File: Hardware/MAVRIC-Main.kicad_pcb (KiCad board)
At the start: 2 copper layers, 0 parts

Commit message: Add basic connector and ChipKit headers
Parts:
- added J1: MTR1, CONN-WM6469CT, F.Cu at (72.4, 109.2)
- added J10: CAM, CONN-WM6469CT, F.Cu at (30.5, 66.0)
- added J11: CK-PWR, HDRV8W38P254_6X1-SMT, B.Cu at (90.2, 101.6)
- added J12: CK-A0, HDRV8W38P254_8X1-SMT, B.Cu at (110.5, 101.6)
- added J13: CK-A1, HDRV8W38P254_8X1-SMT, B.Cu at (133.3, 101.6)
- added J14: CK-COM, HDRV8W38P254_8X1-SMT, B.Cu at (128.3, 53.3)
- added J15: CK-D0, HDRV16W64P254_8X2-SMT, B.Cu at (105.4, 54.6)
- added J16: CK-X0, HDRV16W64P254_8X2-SMT, B.Cu at (146.1, 64.8)
- added J17: CK-D1, HDRV16W64P254_8X2-SMT, B.Cu at (83.6, 54.6)
- added J18: CK-X1, HDRV16W64P254_8X2-SMT, B.Cu at (146.1, 85.1)
- added J2: MTR4, CONN-WM6469CT, F.Cu at (95.2, 109.2)
- added J3: MTR2, CONN-WM6469CT, F.Cu at (118.1, 109.2)
- added J4: MTR5, CONN-WM6469CT, F.Cu at (72.4, 45.7)
- added J5: MTR3, CONN-WM6469CT, F.Cu at (95.2, 45.7)
- added J6: MTR6, CONN-WM6469CT, F.Cu at (118.1, 45.7)
- added J7: VID, CONN-WM6469CT, F.Cu at (141.0, 109.2)
- added J8: DAT, CONN-WM6469CT, F.Cu at (141.0, 45.7)
- added J9: ARM, CONN-WM6469CT, F.Cu at (30.5, 88.9)
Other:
- board outline added: 101.6 x 58.4 mm

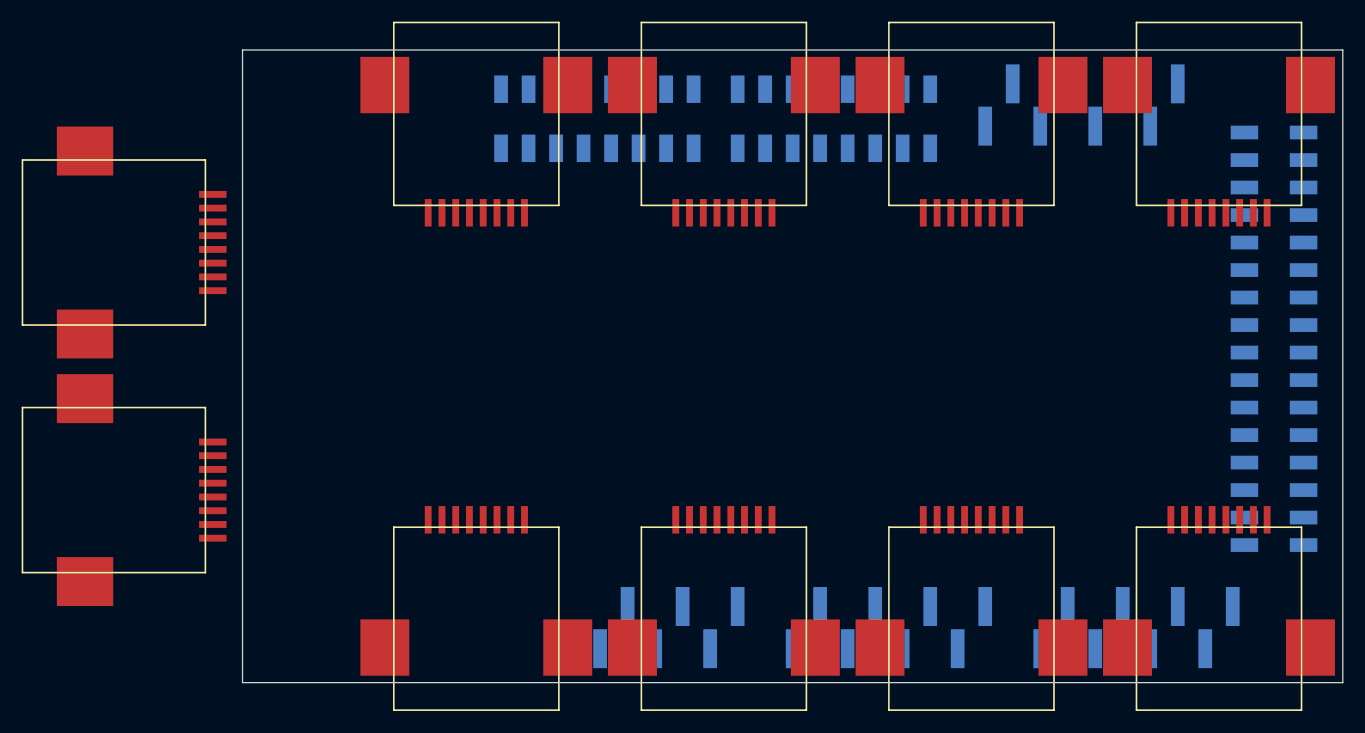
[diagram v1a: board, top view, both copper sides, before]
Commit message: Replace arm and camera connectors with vertical style
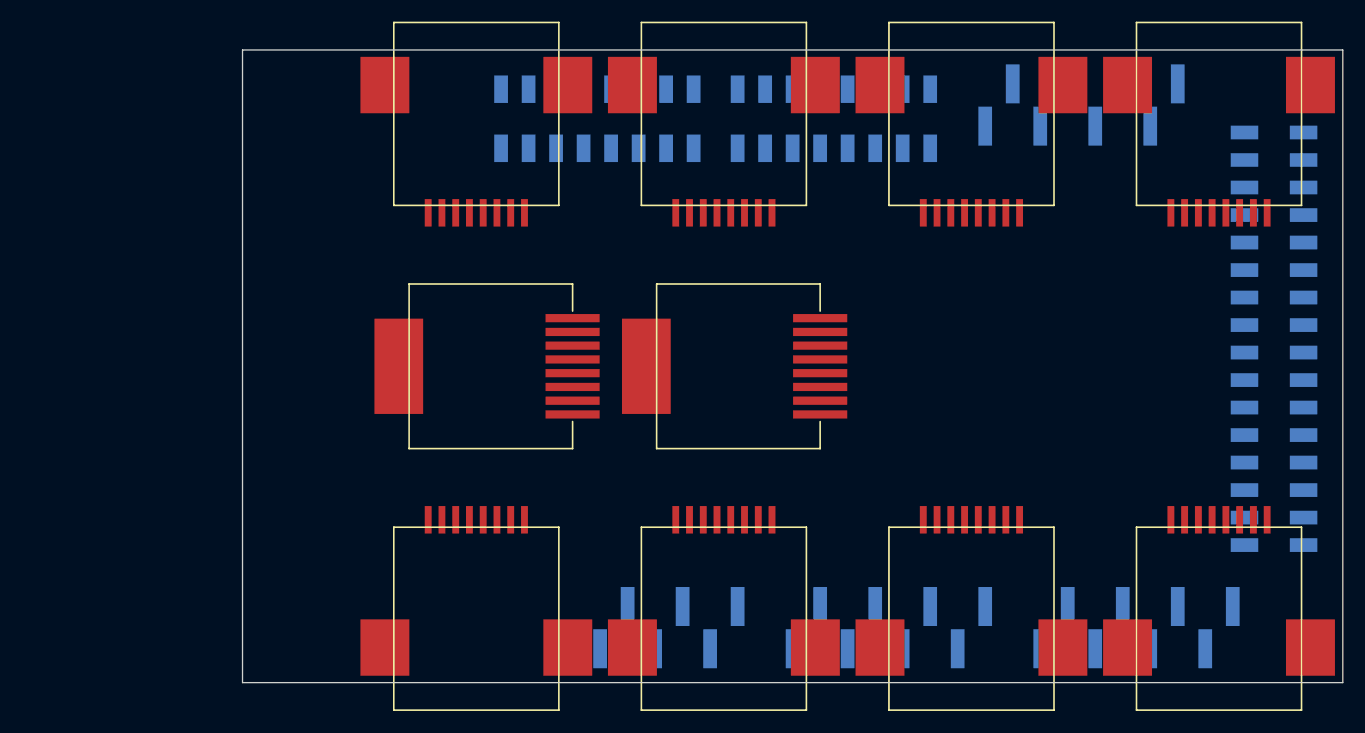
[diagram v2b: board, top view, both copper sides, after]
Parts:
- J10, J9: footprint CONN-WM6469CT -> CONN-WM3553CT
- moved J10 74.5 mm to (104.1, 77.5), turned to 90 degrees
- moved J9 52.1 mm to (81.3, 77.5), turned to 90 degrees
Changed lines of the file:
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@@
     (links 2)
     (no_connects 2)
-    (area 29.976 45.216 153.117474 109.724)
+    (area 50.749999 45.216 153.117474 109.724)
     (thickness 1.6)
     (drawings 4)
@@
     (mod_text_size 1 1)
     (mod_text_width 0.15)
-    (pad_size 1.27 3.6)
+    (pad_size 8.8 4.5)
     (pad_drill 0)
     (pad_to_mask_clearance 0)
@@
     )
   )
-  (module CONN-WM6469CT (layer F.Cu)
-    (at 30.48 88.9 270)
-    (descr "Conn, RJ45")
-    (tags Conn)
-    (fp_text reference J9 (at 0 -11.43 270) (layer F.SilkS) hide
-      (effects (font (size 1 1) (thickness 0.15)))
-    )
-    (fp_text value ARM (at 0 -12.7 270) (layer F.SilkS) hide
-      (effects (font (size 1 1) (thickness 0.15)))
-    )
-    (fp_line (start -7.62 0) (end -7.62 -16.891) (layer F.SilkS) (width 0.15))
-    (fp_line (start -7.62 -16.891) (end 7.62 -16.891) (layer F.SilkS) (width 0.15))
-    (fp_line (start 7.62 -16.891) (end 7.62 0) (layer F.SilkS) (width 0.15))
-    (fp_line (start 7.62 0) (end -7.62 0) (layer F.SilkS) (width 0.15))
-    (pad 1 smd rect (at -4.445 -17.5768 270) (size 0.635 2.54)
-      (layers F.Cu F.Paste F.Mask)
-    )
-    (pad 2 smd rect (at -3.175 -17.5768 270) (size 0.635 2.54)
-      (layers F.Cu F.Paste F.Mask)
-    )
-    (pad 3 smd rect (at -1.905 -17.5768 270) (size 0.635 2.54)
-      (layers F.Cu F.Paste F.Mask)
-    )
-    (pad 4 smd rect (at -0.635 -17.5768 270) (size 0.635 2.54)
-      (layers F.Cu F.Paste F.Mask)
-    )
-    (pad 5 smd rect (at 0.635 -17.5768 270) (size 0.635 2.54)
-      (layers F.Cu F.Paste F.Mask)
-    )
-    (pad 6 smd rect (at 1.905 -17.5768 270) (size 0.635 2.54)
-      (layers F.Cu F.Paste F.Mask)
-    )
-    (pad 7 smd rect (at 3.175 -17.5768 270) (size 0.635 2.54)
-      (layers F.Cu F.Paste F.Mask)
-    )
-    (pad 8 smd rect (at 4.445 -17.5768 270) (size 0.635 2.54)
-      (layers F.Cu F.Paste F.Mask)
-    )
-    (pad "" smd rect (at 8.4455 -5.7785 270) (size 4.5212 5.207)
-      (layers F.Cu F.Paste F.Mask)
-    )
-    (pad "" smd rect (at -8.4455 -5.7785 270) (size 4.5212 5.207)
-      (layers F.Cu F.Paste F.Mask)
-    )
-  )
-  (module CONN-WM6469CT (layer F.Cu)
-    (at 30.48 66.04 270)
-    (descr "Conn, RJ45")
-    (tags Conn)
-    (fp_text reference J10 (at 0 -11.43 270) (layer F.SilkS) hide
-      (effects (font (size 1 1) (thickness 0.15)))
-    )
-    (fp_text value CAM (at 0 -12.7 270) (layer F.SilkS) hide
-      (effects (font (size 1 1) (thickness 0.15)))
-    )
-    (fp_line (start -7.62 0) (end -7.62 -16.891) (layer F.SilkS) (width 0.15))
-    (fp_line (start -7.62 -16.891) (end 7.62 -16.891) (layer F.SilkS) (width 0.15))
-    (fp_line (start 7.62 -16.891) (end 7.62 0) (layer F.SilkS) (width 0.15))
-    (fp_line (start 7.62 0) (end -7.62 0) (layer F.SilkS) (width 0.15))
-    (pad 1 smd rect (at -4.445 -17.5768 270) (size 0.635 2.54)
-      (layers F.Cu F.Paste F.Mask)
-    )
-    (pad 2 smd rect (at -3.175 -17.5768 270) (size 0.635 2.54)
-      (layers F.Cu F.Paste F.Mask)
-    )
-    (pad 3 smd rect (at -1.905 -17.5768 270) (size 0.635 2.54)
-      (layers F.Cu F.Paste F.Mask)
-    )
-    (pad 4 smd rect (at -0.635 -17.5768 270) (size 0.635 2.54)
-      (layers F.Cu F.Paste F.Mask)
-    )
-    (pad 5 smd rect (at 0.635 -17.5768 270) (size 0.635 2.54)
-      (layers F.Cu F.Paste F.Mask)
-    )
-    (pad 6 smd rect (at 1.905 -17.5768 270) (size 0.635 2.54)
-      (layers F.Cu F.Paste F.Mask)
-    )
-    (pad 7 smd rect (at 3.175 -17.5768 270) (size 0.635 2.54)
-      (layers F.Cu F.Paste F.Mask)
-    )
-    (pad 8 smd rect (at 4.445 -17.5768 270) (size 0.635 2.54)
-      (layers F.Cu F.Paste F.Mask)
-    )
-    (pad "" smd rect (at 8.4455 -5.7785 270) (size 4.5212 5.207)
-      (layers F.Cu F.Paste F.Mask)
-    )
-    (pad "" smd rect (at -8.4455 -5.7785 270) (size 4.5212 5.207)
-      (layers F.Cu F.Paste F.Mask)
-    )
-  )
   (module HDRV8W38P254_8X1-SMT (layer B.Cu)
     (at 110.49 101.6)
@@
     )
   )
+  (module CONN-WM3553CT (layer F.Cu)
+    (at 81.28 77.47 90)
+    (descr "Conn, RJ45, SMT, Top")
+    (fp_text reference J9 (at 0 3.81 90) (layer F.SilkS) hide
+      (effects (font (size 1 1) (thickness 0.15)))
+    )
+    (fp_text value ARM (at 0 -3.81 90) (layer F.SilkS) hide
+      (effects (font (size 1 1) (thickness 0.15)))
+    )
+    (fp_line (start -5.1 0) (end -7.6 0) (layer F.SilkS) (width 0.15))
+    (fp_line (start -7.6 0) (end -7.6 -15.1) (layer F.SilkS) (width 0.15))
+    (fp_line (start -7.6 -15.1) (end 7.6 -15.1) (layer F.SilkS) (width 0.15))
+    (fp_line (start 7.6 -15.1) (end 7.6 0) (layer F.SilkS) (width 0.15))
+    (fp_line (start 7.6 0) (end 5.1 0) (layer F.SilkS) (width 0.15))
+    (pad 1 smd rect (at 4.445 0 90) (size 0.76 5)
+      (layers F.Cu F.Paste F.Mask)
+    )
+    (pad 2 smd rect (at 3.175 0 90) (size 0.76 5)
+      (layers F.Cu F.Paste F.Mask)
+    )
+    (pad 3 smd rect (at 1.905 0 90) (size 0.76 5)
+      (layers F.Cu F.Paste F.Mask)
+    )
+    (pad 4 smd rect (at 0.635 0 90) (size 0.76 5)
+      (layers F.Cu F.Paste F.Mask)
+    )
+    (pad 5 smd rect (at -0.635 0 90) (size 0.76 5)
+      (layers F.Cu F.Paste F.Mask)
+    )
+    (pad 6 smd rect (at -1.905 0 90) (size 0.76 5)
+      (layers F.Cu F.Paste F.Mask)
+    )
+    (pad 7 smd rect (at -3.175 0 90) (size 0.76 5)
+      (layers F.Cu F.Paste F.Mask)
+    )
+    (pad 8 smd rect (at -4.445 0 90) (size 0.76 5)
+      (layers F.Cu F.Paste F.Mask)
+    )
+    (pad "" smd rect (at 0 -16.05 90) (size 8.8 4.5)
+      (layers F.Cu F.Paste F.Mask)
+    )
+  )
+  (module CONN-WM3553CT (layer F.Cu)
+    (at 104.14 77.47 90)
+    (descr "Conn, RJ45, SMT, Top")
+    (fp_text reference J10 (at 0 3.81 90) (layer F.SilkS) hide
+      (effects (font (size 1 1) (thickness 0.15)))
+    )
+    (fp_text value CAM (at 0 -3.81 90) (layer F.SilkS) hide
+      (effects (font (size 1 1) (thickness 0.15)))
+    )
+    (fp_line (start -5.1 0) (end -7.6 0) (layer F.SilkS) (width 0.15))
+    (fp_line (start -7.6 0) (end -7.6 -15.1) (layer F.SilkS) (width 0.15))
+    (fp_line (start -7.6 -15.1) (end 7.6 -15.1) (layer F.SilkS) (width 0.15))
+    (fp_line (start 7.6 -15.1) (end 7.6 0) (layer F.SilkS) (width 0.15))
+    (fp_line (start 7.6 0) (end 5.1 0) (layer F.SilkS) (width 0.15))
+    (pad 1 smd rect (at 4.445 0 90) (size 0.76 5)
+      (layers F.Cu F.Paste F.Mask)
+    )
+    (pad 2 smd rect (at 3.175 0 90) (size 0.76 5)
+      (layers F.Cu F.Paste F.Mask)
+    )
+    (pad 3 smd rect (at 1.905 0 90) (size 0.76 5)
+      (layers F.Cu F.Paste F.Mask)
+    )
+    (pad 4 smd rect (at 0.635 0 90) (size 0.76 5)
+      (layers F.Cu F.Paste F.Mask)
+    )
+    (pad 5 smd rect (at -0.635 0 90) (size 0.76 5)
+      (layers F.Cu F.Paste F.Mask)
+    )
+    (pad 6 smd rect (at -1.905 0 90) (size 0.76 5)
+      (layers F.Cu F.Paste F.Mask)
+    )
+    (pad 7 smd rect (at -3.175 0 90) (size 0.76 5)
+      (layers F.Cu F.Paste F.Mask)
+    )
+    (pad 8 smd rect (at -4.445 0 90) (size 0.76 5)
+      (layers F.Cu F.Paste F.Mask)
+    )
+    (pad "" smd rect (at 0 -16.05 90) (size 8.8 4.5)
+      (layers F.Cu F.Paste F.Mask)
+    )
+  )

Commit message: Reload packages for 3D models and fix typo
See AerodyneLabs/KiCadLib@c14934719a961a2749f372fa06ca804ae15d519b for
typo
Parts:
- J11: footprint HDRV8W38P254_6X1-SMT -> HDRV6W38P254_6X1-SMT

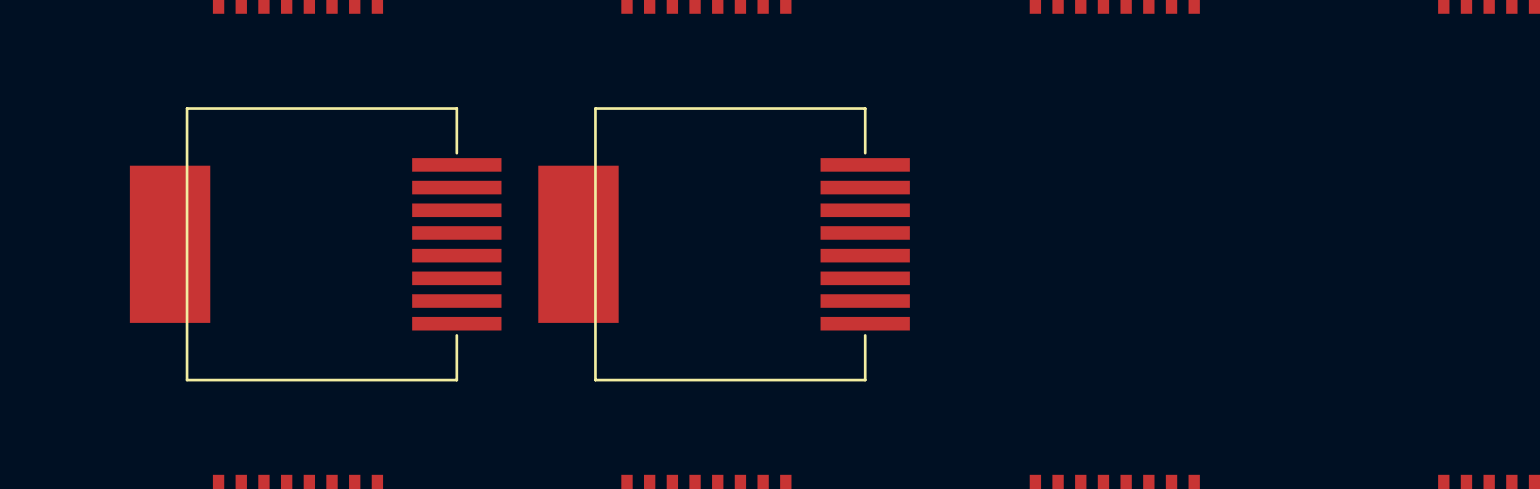
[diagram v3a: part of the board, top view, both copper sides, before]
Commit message: Swap vid/agnd to comply with camera change
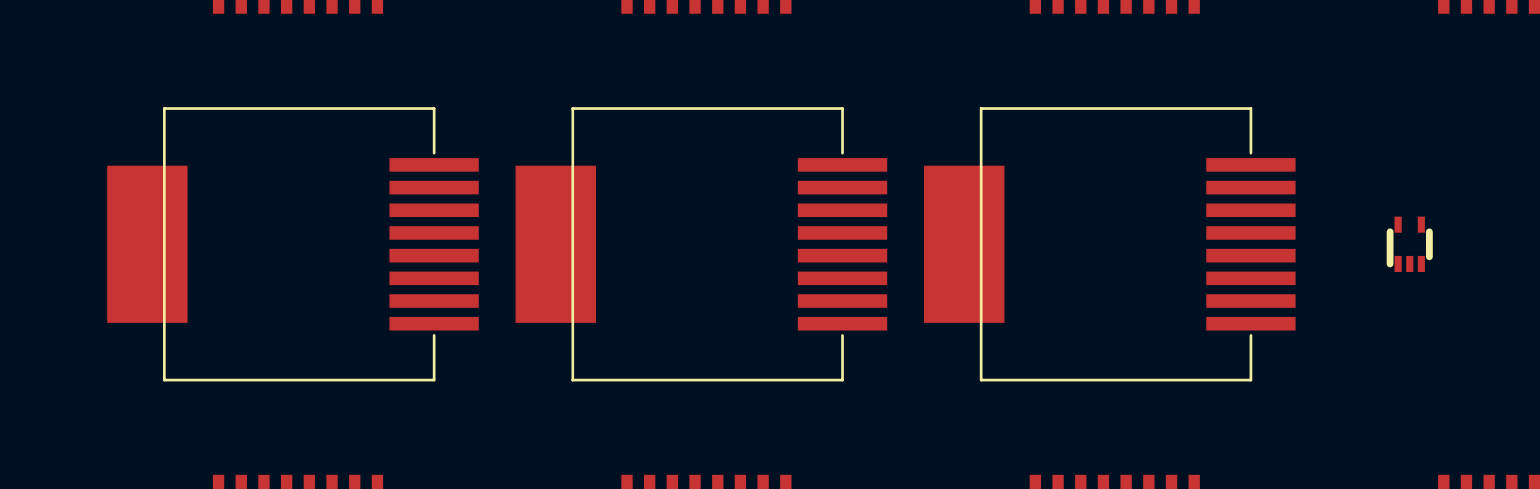
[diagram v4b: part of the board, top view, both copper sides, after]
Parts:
- added J19: GPS, CONN-WM3553CT, F.Cu at (102.9, 77.5)
- added U1: SN74LVC1G125, SOT65P210X110-5N, F.Cu at (134.6, 77.5)
- moved J10 21.6 mm to (125.7, 77.5)
- moved J9 1.27 mm to (80.0, 77.5)
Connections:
- J10 pad 1: (no net) -> /VidGnd
- J10 pad 2: (no net) -> /Video
- J10 pad 3: (no net) -> /TX3
- J10 pad 4: (no net) -> /CamPwr
- J10 pad 5: (no net) -> /CamPwr
- J10 pad 6: (no net) -> /RX3
- J10 pad 7: (no net) -> /CamGnd
- J10 pad 8: (no net) -> /CamGnd
- J11 pad 3: (no net) -> +5V
- J14 pad 3: (no net) -> /RX1
- J14 pad 4: (no net) -> /TX1
- J14 pad 7: (no net) -> /RX3
- J14 pad 8: (no net) -> /TX3
- J15 pad 2: (no net) -> /RX0
- J15 pad 4: (no net) -> /TX0
- J7 pad 1: (no net) -> /Video
- J7 pad 2: (no net) -> /VidGnd
- J7 pad 4: (no net) -> /TxPwr
- J7 pad 5: (no net) -> /TxPwr
- J7 pad 7: (no net) -> /TxGnd
- J7 pad 8: (no net) -> /TxGnd
- J8 pad 1: (no net) -> /TX0
- J8 pad 2: (no net) -> /TxGnd
- J8 pad 3: (no net) -> /RX0
- J8 pad 4: (no net) -> /TxPwr
- J8 pad 5: (no net) -> /TxPwr
- J8 pad 6: (no net) -> /TxGnd
- J8 pad 7: (no net) -> /TxGnd
- J8 pad 8: (no net) -> /TxGnd

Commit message: Rough pin out of most systems
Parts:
- added C1: 0.1uF, CAPC2012, F.Cu at (134.5, 80.5)
- moved J2 67.5 mm to (72.4, 45.7), turned to 180 degrees
- moved J5 67.5 mm to (118.1, 109.2), turned to 0 degrees
- moved J3 22.9 mm to (95.2, 109.2)
- moved J4 22.9 mm to (95.2, 45.7)
- moved U1 0.12 mm to (134.5, 77.5)
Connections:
- J1 pad 1: (no net) -> /MotorTx
- J1 pad 2: (no net) -> /CK85
- J1 pad 3: (no net) -> +3.3V
- J1 pad 4: (no net) -> /CK84
- J1 pad 5: (no net) -> /CK83
- J1 pad 6: (no net) -> /CK82
- J1 pad 7: (no net) -> /A1
- J1 pad 8: (no net) -> GND
- J10 pad 4: /CamPwr -> +BATT
- J10 pad 5: /CamPwr -> +BATT
- J10 pad 7: /CamGnd -> GND
- J10 pad 8: /CamGnd -> GND
- J11 pad 2: (no net) -> +3.3V
- J11 pad 6: (no net) -> +BATT
- J12 pad 2: (no net) -> /A1
- J12 pad 3: (no net) -> /A2
- J12 pad 4: (no net) -> /A3
- J12 pad 5: (no net) -> /A4
- J12 pad 6: (no net) -> /A5
- J12 pad 7: (no net) -> /A6
- J15 pad 10: (no net) -> /CK4
- J15 pad 11: (no net) -> /CK75
- J15 pad 12: (no net) -> /CK5
- J15 pad 13: (no net) -> /CK76
- J15 pad 14: (no net) -> /CK6
- J15 pad 15: (no net) -> /CK77
- J15 pad 16: (no net) -> /CK7
- J15 pad 6: (no net) -> /CK2
- J15 pad 8: (no net) -> /CK3
- J15 pad 9: (no net) -> /CK74
- J17 pad 1: (no net) -> /CK78
- J17 pad 10: (no net) -> /CK12
- J17 pad 11: (no net) -> /CK83
- J17 pad 12: (no net) -> /A4
- J17 pad 13: (no net) -> /CK84
- J17 pad 15: (no net) -> /CK85
- J17 pad 2: (no net) -> /CK8
- J17 pad 3: (no net) -> /CK79
- J17 pad 4: (no net) -> /CK9
- J17 pad 5: (no net) -> /CK80
- J17 pad 6: (no net) -> /CK10
- J17 pad 7: (no net) -> /CK81
- J17 pad 8: (no net) -> /CK11
- J17 pad 9: (no net) -> /CK82
- J19 pad 2: (no net) -> GND
- J2 pad 1: (no net) -> /MotorTx
- J2 pad 2: (no net) -> /CK10
- J2 pad 3: (no net) -> +3.3V
- J2 pad 5: (no net) -> /CK11
- J2 pad 6: (no net) -> /CK12
- J2 pad 7: (no net) -> /A4
- J2 pad 8: (no net) -> GND
- J3 pad 1: (no net) -> /MotorTx
- J3 pad 2: (no net) -> /CK81
- J3 pad 3: (no net) -> +3.3V
- J3 pad 4: (no net) -> /CK80
- J3 pad 5: (no net) -> /CK79
- J3 pad 6: (no net) -> /CK78
- J3 pad 7: (no net) -> /A2
- J3 pad 8: (no net) -> GND
- J4 pad 1: (no net) -> /MotorTx
- J4 pad 2: (no net) -> /CK6
- J4 pad 3: (no net) -> +3.3V
- J4 pad 4: (no net) -> /CK7
- J4 pad 5: (no net) -> /CK8
- J4 pad 6: (no net) -> /CK9
- J4 pad 7: (no net) -> /A5
- J4 pad 8: (no net) -> GND
- J5 pad 1: (no net) -> /MotorTx
- J5 pad 2: (no net) -> /CK77
- J5 pad 3: (no net) -> +3.3V
- J5 pad 4: (no net) -> /CK76
- J5 pad 5: (no net) -> /CK75
- J5 pad 6: (no net) -> /CK74
- J5 pad 7: (no net) -> /A3
- J5 pad 8: (no net) -> GND
- J6 pad 1: (no net) -> /MotorTx
- J6 pad 2: (no net) -> /CK2
- J6 pad 3: (no net) -> +3.3V
- J6 pad 4: (no net) -> /CK3
- J6 pad 5: (no net) -> /CK4
- J6 pad 6: (no net) -> /CK5
- J6 pad 7: (no net) -> /A6
- J6 pad 8: (no net) -> GND
- J7 pad 4: /TxPwr -> +BATT
- J7 pad 5: /TxPwr -> +BATT
- J7 pad 7: /TxGnd -> GND
- J7 pad 8: /TxGnd -> GND
- J8 pad 2: /TxGnd -> GND
- J8 pad 4: /TxPwr -> +BATT
- J8 pad 5: /TxPwr -> +BATT
- J8 pad 6: /TxGnd -> GND
- J8 pad 7: /TxGnd -> GND
- J8 pad 8: /TxGnd -> GND
- U1 pad 1: (no net) -> +5V
- U1 pad 3: (no net) -> GND
- U1 pad 4: (no net) -> /MotorTx
- U1 pad 5: (no net) -> +5V
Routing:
- added copper zone on B.Cu, net GND

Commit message: Finish 1v0 circuit board!
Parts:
- added C2: 0.1uF, CAPC2012, F.Cu at (59.7, 97.8)
- added D1: LED, LEDC2012, F.Cu at (52.1, 97.8)
- added J20: CONN-DC, CONN-JST-XH-2, F.Cu at (50.8, 91.4)
- added R1: 36k, RESC2012, F.Cu at (55.9, 97.8)
- added R2: 10k, RESC2012, F.Cu at (57.8, 97.8)
- added R3: R, RESC2012, F.Cu at (54.0, 97.8)
- moved C1 24.5 mm to (129.5, 56.5), turned to 180 degrees
- moved J10 22.9 mm to (102.9, 77.5)
- moved J19 22.9 mm to (125.7, 77.5)
- moved U1 17.9 mm to (129.5, 60.3), turned to 180 degrees
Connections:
- J1 pad 7: /A1 -> /A2
- J12 pad 1: (no net) -> /A0
- J14 pad 5: (no net) -> /RX2
- J14 pad 6: (no net) -> /TX2
- J15 pad 11: /CK75 -> (no net)
- J15 pad 13: /CK76 -> (no net)
- J15 pad 15: /CK77 -> (no net)
- J15 pad 3: (no net) -> /CK71
- J15 pad 5: (no net) -> /CK72
- J15 pad 7: (no net) -> /CK73
- J17 pad 12: /A4 -> /CK13
- J2 pad 4: (no net) -> /CK11
- J2 pad 5: /CK11 -> /CK12
- J2 pad 6: /CK12 -> /CK13
- J2 pad 7: /A4 -> /A1
- J3 pad 7: /A2 -> /A4
- J4 pad 7: /A5 -> /A3
- J5 pad 2: /CK77 -> /CK74
- J5 pad 4: /CK76 -> /CK73
- J5 pad 5: /CK75 -> /CK72
- J5 pad 6: /CK74 -> /CK71
- J5 pad 7: /A3 -> /A6
- J6 pad 7: /A6 -> /A5
- J7 pad 1: /Video -> /VidGnd
- J7 pad 2: /VidGnd -> /Video
- J9 pad 1: (no net) -> /TX2
- J9 pad 2: (no net) -> GND
- J9 pad 3: (no net) -> /RX2
- J9 pad 6: (no net) -> GND
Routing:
- net +BATT: track 0.00 -> 192.0 mm, vias 0 -> 6
- net /MotorTx: track 0.00 -> 137.5 mm, vias 0 -> 8
- net +5V: track 0.00 -> 110.8 mm, vias 0 -> 1
- net /A1: track 0.00 -> 68.7 mm, vias 0 -> 1
- net /RX2: track 0.00 -> 67.8 mm, vias 0 -> 1
- net /TX2: track 0.00 -> 60.4 mm, vias 0 -> 1
- net /Video: track 0.00 -> 55.7 mm
- net /VidGnd: track 0.00 -> 55.0 mm
- net /RX3: track 0.00 -> 51.5 mm, vias 0 -> 1
- net /A3: track 0.00 -> 50.2 mm, vias 0 -> 1
- net /TX0: track 0.00 -> 49.1 mm, vias 0 -> 1
- net /A0: track 0.00 -> 47.7 mm, vias 0 -> 1
- net /RX0: track 0.00 -> 43.6 mm, vias 0 -> 1
- net GND: track 0.00 -> 42.9 mm, vias 0 -> 5
- net /A2: track 0.00 -> 41.5 mm, vias 0 -> 1
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- added copper zone on B.Cu, net +3.3V
- added copper zone on F.Cu, net GND
- removed copper zone on B.Cu, net GND
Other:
- net class Batt added: clearance 0.2032, trace_width 0.4064, via_dia 0.889, via_drill 0.635
- net class Default: clearance 0.254 -> 0.1524; trace_width 0.254 -> 0.2032; via_dia 0.889 -> 0.7366; via_drill 0.635 -> 0.3556
- rule trace_clearance: 0.254 -> 0.1524
- rule trace_min: 0.254 -> 0.2032
- rule via_min_drill: 0.508 -> 0.3302
- rule via_min_size: 0.889 -> 0.6858
